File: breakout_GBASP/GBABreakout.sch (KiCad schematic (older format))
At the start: 17 parts, among them J1 Conn_01x16, J10 TP8, J11 TP3, J12 TP2, J13 S02, J14 S01, J15 CK1, J16 EX1, J17 GND, J2 VCC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

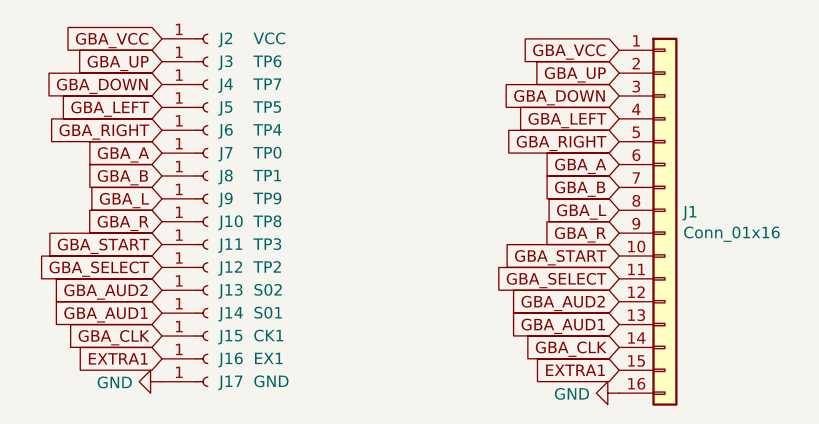
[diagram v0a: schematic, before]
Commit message: some minor changes
* improved SP compatibility
* changed via diameter to 0.6mm and holesize to 0.3mm
* updated Readme
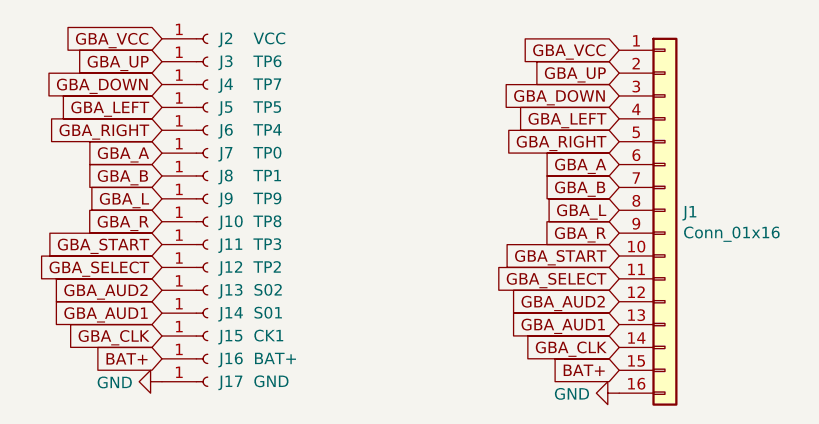
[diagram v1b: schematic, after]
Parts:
- J1: footprint OFFSET:JUSHUO_AFC07-S16FCC-00 -> Connector_FFC-FPC:TE_1-1734839-6_1x16-1MP_P0.5mm_Horizontal
- J16: value EX1 -> BAT+
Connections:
- net EXTRA1 renamed BAT+
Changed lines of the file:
@@
 F 0 "J1" H 5080 2142 50  0000 L CNN
 F 1 "Conn_01x16" H 5080 2051 50  0000 L CNN
-F 2 "OFFSET:JUSHUO_AFC07-S16FCC-00" H 5000 2150 50  0001 C CNN
+F 2 "Connector_FFC-FPC:TE_1-1734839-6_1x16-1MP_P0.5mm_Horizontal" H 5000 2150 50  0001 C CNN
 F 3 "~" H 5000 2150 50  0001 C CNN
 	1    5000 2150
@@
 GBA_L
 Text GLabel 4800 2850 0    50   Input ~ 0
-EXTRA1
+BAT+
 Text GLabel 2800 2800 0    50   Input ~ 0
-EXTRA1
+BAT+
 $Comp
 L power:GND #PWR0102
@@
 P 3000 2800
 F 0 "J16" H 3050 2800 50  0000 L CNN
-F 1 "EX1" H 3200 2800 50  0000 L CNN
+F 1 "BAT+" H 3200 2800 50  0000 L CNN
 F 2 "OFFSET:SOLDER_PAD" H 3000 2800 50  0001 C CNN
 F 3 "~" H 3000 2800 50  0001 C CNN

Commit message: updated shield
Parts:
- J16: value BAT+ -> EX1
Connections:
- net BAT+ renamed EX1
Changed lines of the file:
@@
 GBA_L
 Text GLabel 4800 2850 0    50   Input ~ 0
-BAT+
+EX1
 Text GLabel 2800 2800 0    50   Input ~ 0
-BAT+
+EX1
 $Comp
 L power:GND #PWR0102
@@
 P 3000 2800
 F 0 "J16" H 3050 2800 50  0000 L CNN
-F 1 "BAT+" H 3200 2800 50  0000 L CNN
+F 1 "EX1" H 3200 2800 50  0000 L CNN
 F 2 "OFFSET:SOLDER_PAD" H 3000 2800 50  0001 C CNN
 F 3 "~" H 3000 2800 50  0001 C CNN
